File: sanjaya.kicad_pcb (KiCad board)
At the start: 2 copper layers, 82 parts, among them J1 PWR_SUPPLY, J10 Bat_Bak_Byp_Gnd, J11 USB_B_Micro_OUT, J12 ON_Switch, J13 Raspberry_Pi_2_3, J14 Fan, J15 RS232, J16 RS485, J17 I2C, J18 Bat_Bak_Byp_Vcc, J2 Digital_Input_Signals, J3 Digital_Input_Gnd, J4 Screw_Terminal_01x03, J5 Screw_Terminal_01x03, J6 Analog_RSense, J7 Analog_420, J8 Supply_Safety_Bypass, J9 USB_B_Micro_IN, K1 Songle-SRD, K2 Songle-SRD, Q1 Q_PMOS_GSD, Q2 FDC021N30, SW2 SW_DIP_x04, U1 74HC14, U2 MCP9700T-ETT, U3 TPS2400BVR, U4 ULN2803A, U5 MCP3428, U6 TLP291-4, U7 MAX232, U8 SN65HVD75DR

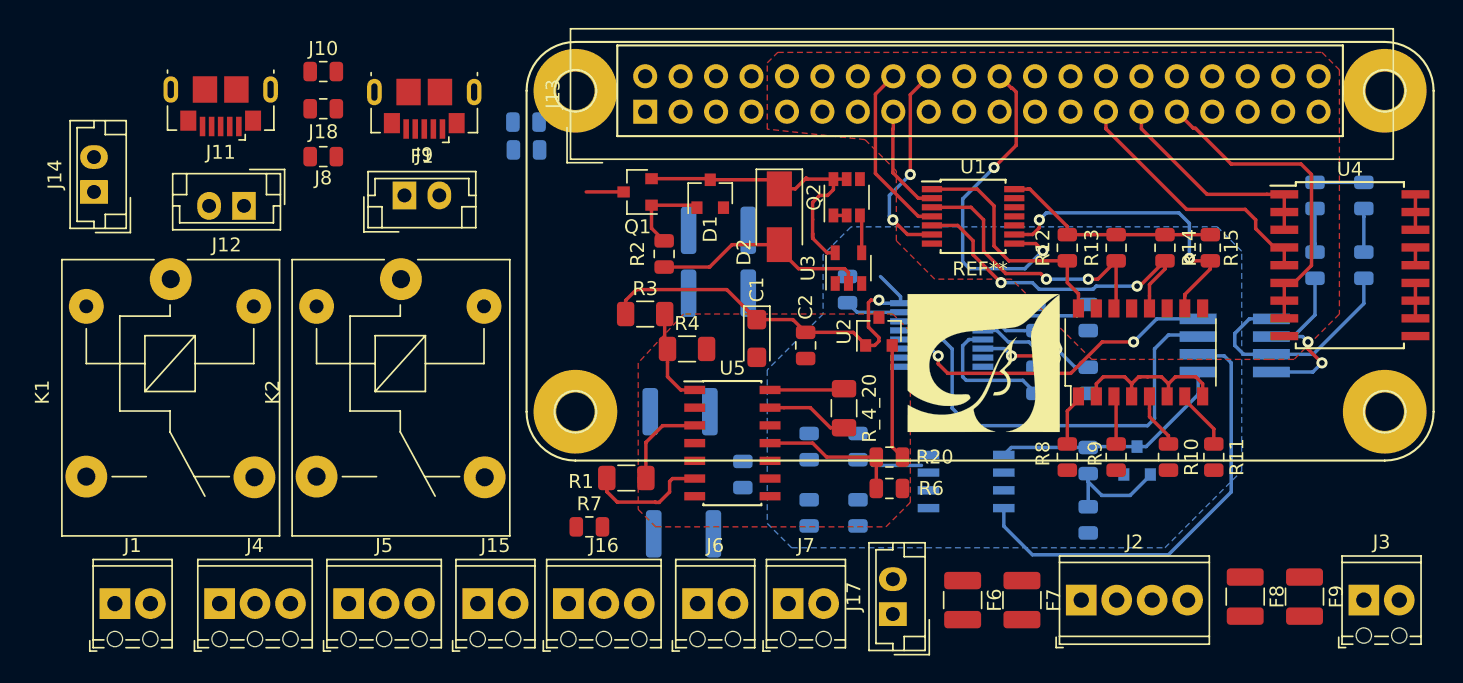
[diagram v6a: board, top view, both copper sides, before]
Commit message: Changed USB footprints and did some more routing
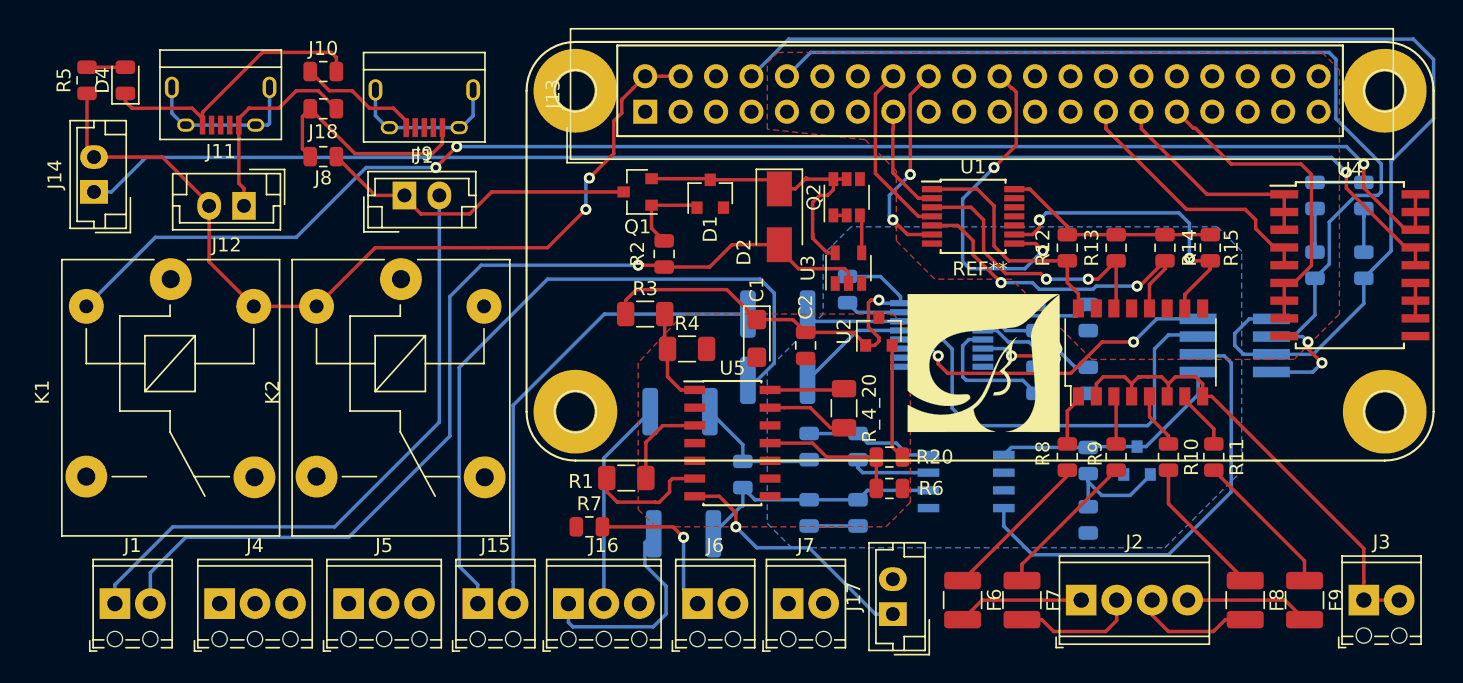
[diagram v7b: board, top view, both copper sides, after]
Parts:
- D4, R5: moved to F.Cu
- J11, J9: footprint Connector_USB:USB_Micro-B_GCT_USB3076-30-A -> Connector_USB:USB_Micro-B
- moved R5 31.6 mm to (76.8, 87.2), turned to 90 degrees
- moved D4 29.2 mm to (79.5, 87.2), turned to 90 degrees
- moved F5 7.56 mm to (126.2, 108.8)
- moved F4 7.35 mm to (126.2, 104.0)
- moved F8 0.25 mm to (159.8, 124.5)
- moved F9 0.25 mm to (164.0, 124.5)
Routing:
- net Net-(K1-Pad2): track 2.54 -> 106.0 mm, vias 0 -> 3
- net Net-(J14-Pad1): track 1.27 -> 100.3 mm, vias 0 -> 1
- net /rPi/UART_TX: track 16.7 -> 85.1 mm
- net /rPi/5V_In: track 0.00 -> 63.6 mm, vias 0 -> 2
- net /powerSupply/Gnd_In: track 15.7 -> 78.6 mm, vias 0 -> 1
- net /rPi/UART_RX: track 15.0 -> 75.2 mm
- net /serial/RS232_RX: track 0.00 -> 50.5 mm
- net /powerSupply/V_adapter_out: track 0.00 -> 45.7 mm
- net /serial/RS232_TX: track 0.00 -> 33.7 mm
- net /DGND: track 4.08 -> 28.1 mm
- net /digitalSensing/Gnd_in: track 12.5 -> 34.8 mm
- net Net-(F1-Pad1): track 2.68 -> 23.0 mm
- net Net-(C9-Pad2): track 0.00 -> 18.6 mm
- net /analogSensing/SDA: track 0.00 -> 18.3 mm, vias 0 -> 1
- net Net-(C10-Pad1): track 0.00 -> 18.2 mm
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
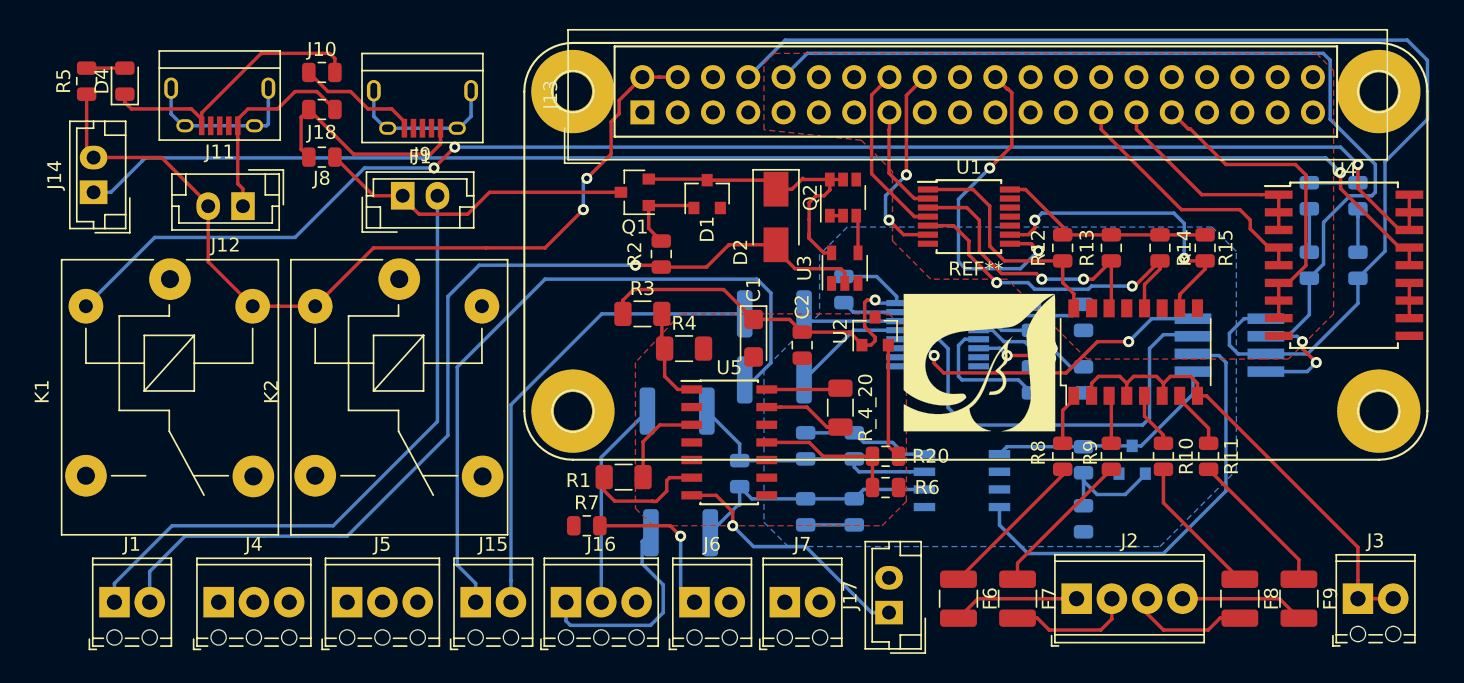
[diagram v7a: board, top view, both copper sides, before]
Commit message: Some more routing done. Only 3-4 nets remaining to be routed
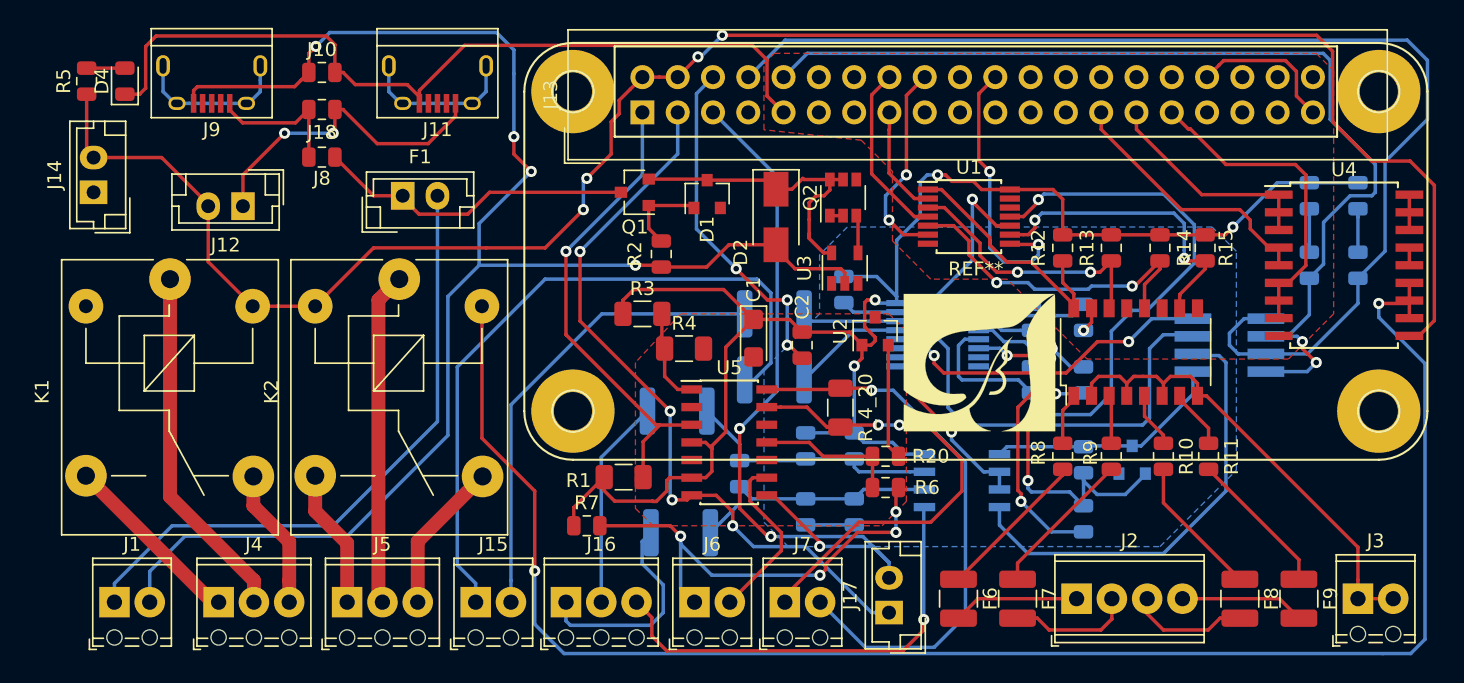
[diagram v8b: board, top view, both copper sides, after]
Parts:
- J11: value USB_B_Micro_OUT -> Board_PwrIn
- J9: value USB_B_Micro_IN -> To_PwrBank
- moved G*** 23.7 mm to (99.2, 109.5)
- moved J11 15.8 mm to (102.0, 87.5)
- moved J9 15.3 mm to (85.8, 87.5)
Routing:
- net Net-(K2-Pad5): track 2.54 -> 120.2 mm, vias 0 -> 2
- net Net-(K1-Pad2): track 106.0 -> 2.54 mm, vias 3 -> 0
- net /DGND: track 28.1 -> 130.1 mm, vias 0 -> 4
- net Net-(J14-Pad1): track 100.3 -> 1.27 mm, vias 1 -> 0
- net /rPi/5V_In: track 63.6 -> 138.7 mm, vias 2 -> 4
- net /analogSensing/SCL: track 0.00 -> 56.0 mm, vias 0 -> 3
- net /3V3: track 68.8 -> 121.5 mm, vias 1 -> 4
- net Net-(C4-Pad1): track 8.47 -> 54.9 mm, vias 0 -> 3
- net /AGND: track 0.00 -> 37.3 mm, vias 0 -> 3
- net /powerSupply/Gnd_In: track 78.6 -> 114.4 mm, vias 1 -> 4
- net /analogSensing/SDA: track 18.3 -> 53.4 mm, vias 1 -> 4
- net /analogSensing/420-: track 5.34 -> 40.3 mm, vias 0 -> 1
- net Net-(U1-Pad10): track 0.00 -> 29.4 mm, vias 0 -> 3
- net /analogSensing/420+: track 5.90 -> 34.3 mm, vias 0 -> 2
- net /3V3_Net+: track 6.56 -> 34.3 mm, vias 0 -> 1
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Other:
- net class AC Signals added: clearance 0.2, trace_width 1, via_dia 0.8, via_drill 0.4
